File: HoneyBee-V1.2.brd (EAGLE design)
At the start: 49.2 x 49.5 mm, 48 parts, among them IC2 CA3130EZLMP, Q1 2N5457

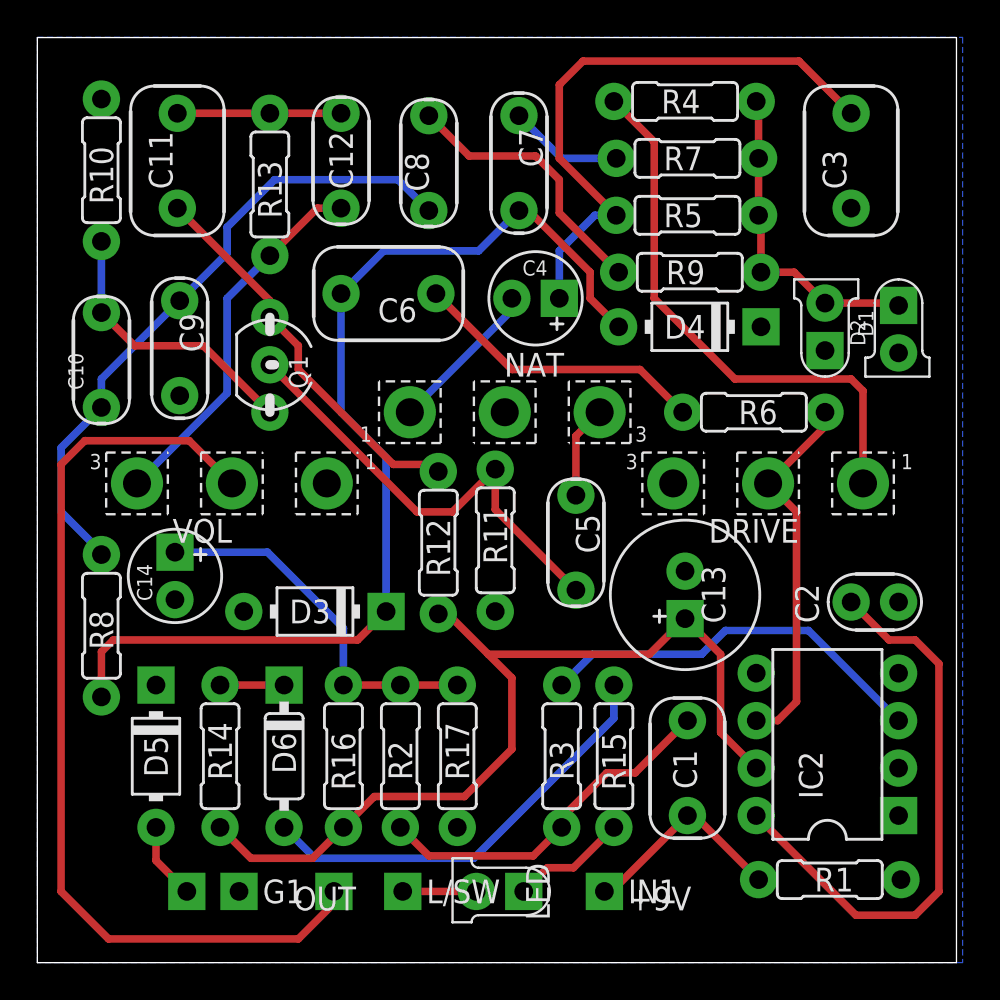
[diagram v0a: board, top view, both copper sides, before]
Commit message: Added SMD Fet layout
Added FET pads to layout. This is version 1.2
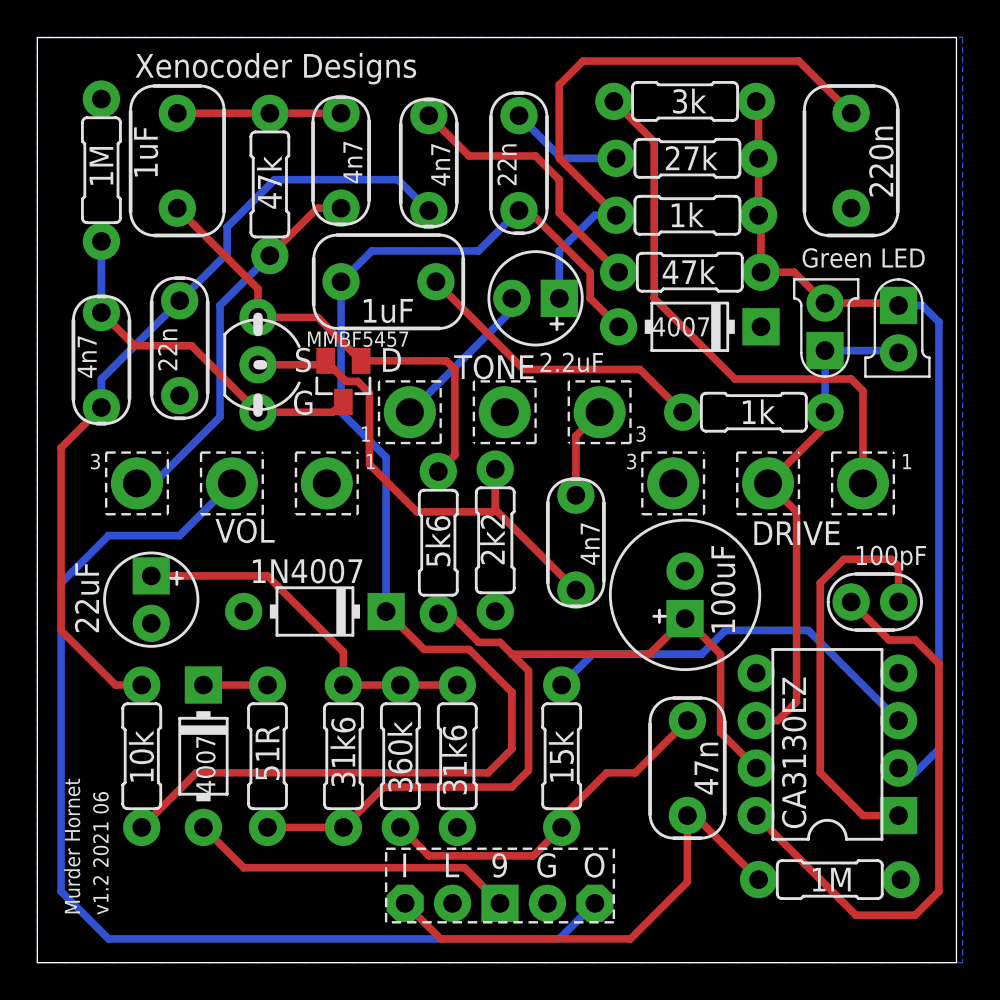
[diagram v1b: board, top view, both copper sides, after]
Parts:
- removed +9V: +9V(T), mb_supply:SQUARE
- removed D6: 5v1 Zener, mb_diodes:DO35-3
- removed G1: GND(T), mb_supply:SQUARE
- removed IN1: IN(T), mb_supply:SQUARE
- removed L/SW: (no value), mb_supply:SQUARE
- removed LED: 3mm, mb_diodes:LED3MM
- removed OUT: OUT(T), mb_supply:SQUARE
- removed R15: 1k, mb_resistors:R0207/3
- added U$1: MMBF5457, xc_library:SOT23
- added U$2: BOARDLINK, xc_library:BOARDLINK
- D4, D5: value 1N4007 -> 4007
- IC2: value CA3130EZLMP -> CA3130EZ
- moved R8 7.31 mm to (5.59, 11.0)
- moved D5 2.54 mm to (8.89, 11.0)
- moved R14 2.54 mm to (12.3, 11.0)
- moved C14 1.80 mm to (6.10, 19.4)
- moved Q1 0.63 mm to (11.8, 32.0)
- moved C6 0.63 mm to (18.8, 36.4)
- renumbered NAT to TONE
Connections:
- removed net +9V: +9V.1, D5.A
- removed net IN: C1.1, IN1.1, R1.2
- removed net OUT: OUT.1, VOL.2
- net GND: now also U$2.4; no longer G1.1
- net N$16: now also U$1.3
- net N$17: now also U$1.2
- net N$18: now also U$1.1
- net N$20: now also C1.1, R1.2, U$2.1; no longer LED.A, R15.2
- net N$23: no longer D6.C
- net N$24: now also D5.A, U$2.3; no longer D6.A, R15.1
- net N$25: now also U$2.5, VOL.2; no longer L/SW.1, LED.K
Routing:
- net N$25: track 3.94 -> 58.3 mm
- net OUT: track 50.6 -> 0.00 mm
- net N$4: track 17.5 -> 45.7 mm
- net N$10: track 0.00 -> 22.1 mm
- net N$20: track 6.25 -> 26.0 mm
- net N$12: track 56.7 -> 71.6 mm
- net IN: track 11.4 -> 0.00 mm
- net N$14: track 34.6 -> 43.3 mm
- net N$8: track 20.0 -> 27.3 mm
- net N$24: track 23.2 -> 17.6 mm
- net N$16: track 15.0 -> 19.2 mm
- net +9V: track 4.11 -> 0.00 mm
- net N$18: track 21.1 -> 25.2 mm
- net VC: track 48.8 -> 46.3 mm
- net N$17: track 24.5 -> 26.7 mm
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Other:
- board text added: "Green LED"
- board text added: "Murder Hornet"
- board text added: "Xenocoder Designs"
- board text added: "v1.2 2021 06"
